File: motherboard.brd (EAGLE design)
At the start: 100 x 80 mm, 23 parts, among them U1 MC34063DIP

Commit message: Fix
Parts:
- moved I2C 1.27 mm to (96.5, 72.4)
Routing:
- net RX: track 110.6 -> 109.2 mm
- net TX: track 103.0 -> 101.8 mm
- net GND: track 346.7 -> 345.5 mm
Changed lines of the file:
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@@
 <element name="CON9" library="con-amp" package="SIMM22" value="" x="67.31" y="41.91" rot="R90"/>
 <element name="CON10" library="con-amp" package="SIMM22" value="" x="74.93" y="41.91" rot="R90"/>
-<element name="I2C" library="SparkFun-Connectors" package="AUDIO-JACK" value="" x="96.52" y="73.66" rot="R180"/>
+<element name="I2C" library="SparkFun-Connectors" package="AUDIO-JACK" value="" x="96.52" y="72.39" rot="R180"/>
 <element name="PWR" library="con-jack" package="DCJ0202" value="DCJ0202" x="88.9" y="59.69" rot="R90">
 <attribute name="OC_NEWARK" value="unknown" x="88.9" y="59.69" size="1.778" layer="27" rot="R90" display="off"/>
@@
 <wire x1="36.83" y1="50.8" x2="29.21" y2="50.8" width="1.4224" layer="16"/>
 <wire x1="74.93" y1="50.8" x2="81.28" y2="50.8" width="1.4224" layer="16"/>
-<wire x1="81.28" y1="50.8" x2="81.28" y2="68.66" width="1.4224" layer="16"/>
+<wire x1="81.28" y1="50.8" x2="81.28" y2="67.39" width="1.4224" layer="16"/>
 <contactref element="I2C" pad="RING"/>
-<wire x1="91.52" y1="68.66" x2="81.28" y2="68.66" width="1.4224" layer="16"/>
+<wire x1="91.52" y1="67.39" x2="81.28" y2="67.39" width="1.4224" layer="16"/>
 </signal>
 <signal name="RX">
@@
 <wire x1="67.31" y1="53.34" x2="74.93" y2="53.34" width="1.4224" layer="16"/>
 <wire x1="74.93" y1="53.34" x2="78.74" y2="53.34" width="1.4224" layer="16"/>
-<wire x1="78.74" y1="53.34" x2="78.74" y2="78.66" width="1.4224" layer="16"/>
+<wire x1="78.74" y1="53.34" x2="78.74" y2="77.39" width="1.4224" layer="16"/>
 <contactref element="I2C" pad="TIP"/>
-<wire x1="91.52" y1="78.66" x2="78.74" y2="78.66" width="1.4224" layer="16"/>
-<wire x1="78.74" y1="78.66" x2="78.74" y2="78.74" width="1.4224" layer="16"/>
+<wire x1="78.74" y1="73.58" x2="78.74" y2="77.47" width="0" layer="19" extent="1-16"/>
+<wire x1="91.52" y1="77.39" x2="78.74" y2="77.39" width="1.4224" layer="16"/>
+<wire x1="78.74" y1="77.39" x2="78.74" y2="73.58" width="0" layer="19" extent="1-16"/>
 </signal>
 <signal name="GND">
@@
 <wire x1="95.25" y1="40.64" x2="97.79" y2="40.64" width="1.4224" layer="16"/>
 <wire x1="97.79" y1="40.64" x2="97.79" y2="53.34" width="1.4224" layer="16"/>
-<wire x1="97.79" y1="53.34" x2="97.79" y2="73.66" width="1.4224" layer="16"/>
-<wire x1="97.79" y1="73.66" x2="96.52" y2="73.66" width="1.4224" layer="16"/>
+<wire x1="97.79" y1="53.34" x2="97.79" y2="72.39" width="1.4224" layer="16"/>
+<wire x1="97.79" y1="72.39" x2="96.52" y2="72.39" width="1.4224" layer="16"/>
 <wire x1="93.98" y1="53.34" x2="97.79" y2="53.34" width="1.4224" layer="16"/>
 <wire x1="29.21" y1="15.24" x2="36.83" y2="15.24" width="1.4224" layer="16"/>

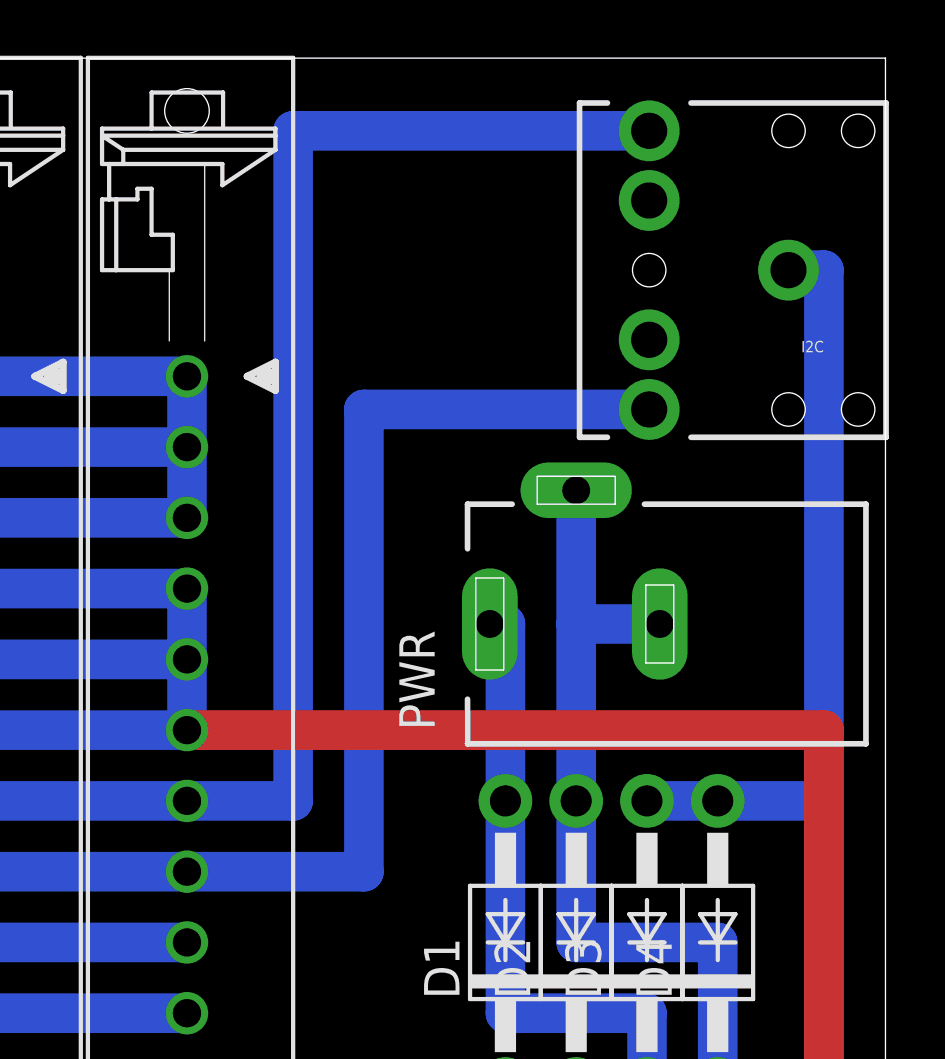
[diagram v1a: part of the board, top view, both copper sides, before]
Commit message: Added 3.3v regulator and circuit
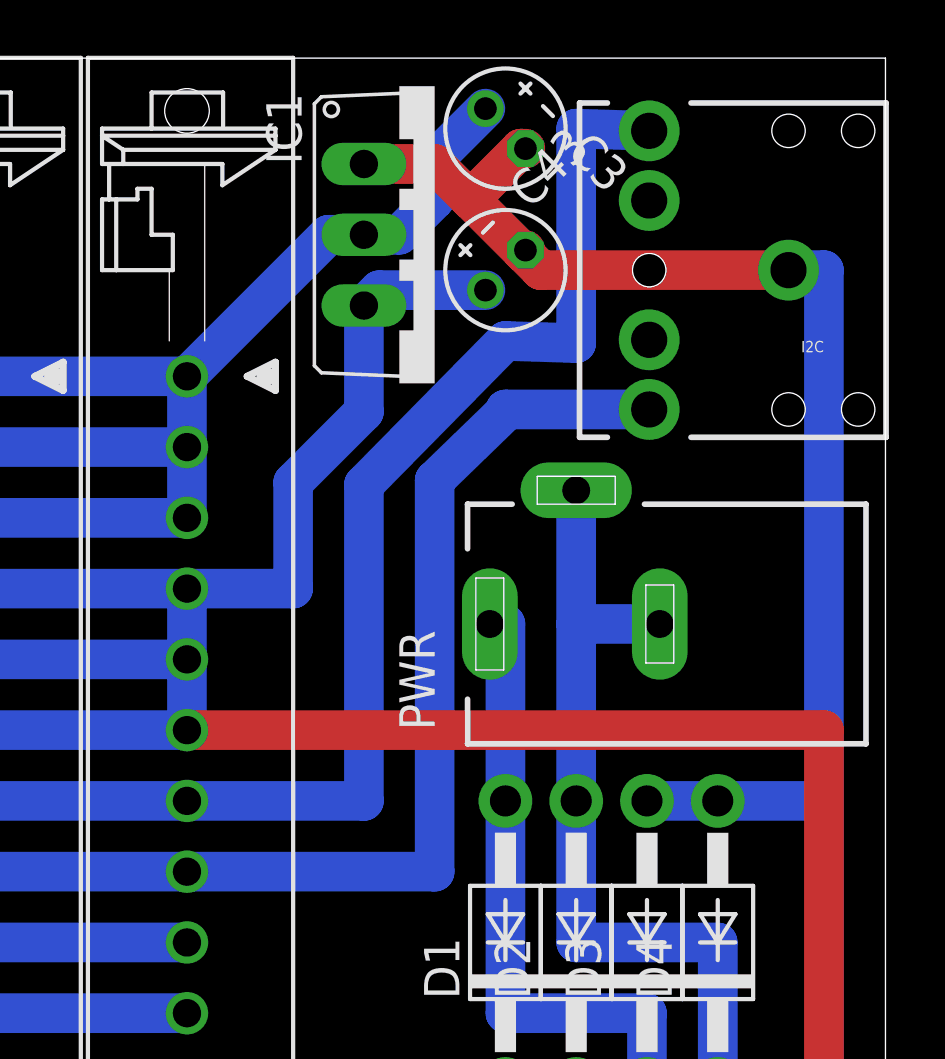
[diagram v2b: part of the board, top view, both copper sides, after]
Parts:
- added C3, C43: (no value), rcl:E2-4
- added IC1: MC33269T-3.3, linear:TO220V
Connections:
- net +3V3: now also C3.+, IC1.2
- net +5V: now also C43.+, IC1.3
- net GND: now also C3.-, C43.-, IC1.1
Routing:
- net GND: track 345.5 -> 365.2 mm
- net +5V: track 293.3 -> 313.0 mm
- net +3V3: track 210.8 -> 226.4 mm
- net RX: track 109.2 -> 106.4 mm
- net TX: track 101.8 -> 100.3 mm
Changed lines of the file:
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@@
 <element name="L1" library="rcl" package="0204/7" value="220uH" x="95.25" y="27.94" rot="R270"/>
 <element name="C2" library="rcl" package="E3,5-8" value="" x="92.71" y="8.89" rot="R45"/>
+<element name="IC1" library="linear" package="TO220V" value="MC33269T-3.3" x="83.82" y="73.66" rot="R270"/>
+<element name="C3" library="rcl" package="E2-4" value="" x="86.36" y="77.47" rot="R315"/>
+<element name="C43" library="rcl" package="E2-4" value="" x="86.36" y="72.39" rot="R45"/>
 </elements>
 <signals>
@@
 <wire x1="44.45" y1="50.8" x2="36.83" y2="50.8" width="1.4224" layer="16"/>
 <wire x1="36.83" y1="50.8" x2="29.21" y2="50.8" width="1.4224" layer="16"/>
-<wire x1="74.93" y1="50.8" x2="81.28" y2="50.8" width="1.4224" layer="16"/>
-<wire x1="81.28" y1="50.8" x2="81.28" y2="67.39" width="1.4224" layer="16"/>
+<wire x1="74.93" y1="50.8" x2="83.82" y2="50.8" width="1.4224" layer="16"/>
+<wire x1="83.82" y1="50.8" x2="83.82" y2="64.85" width="1.4224" layer="16"/>
 <contactref element="I2C" pad="RING"/>
-<wire x1="91.52" y1="67.39" x2="81.28" y2="67.39" width="1.4224" layer="16"/>
+<wire x1="91.52" y1="67.39" x2="86.36" y2="67.39" width="1.4224" layer="16"/>
+<wire x1="86.36" y1="67.39" x2="86.36" y2="67.31" width="1.4224" layer="16"/>
+<wire x1="86.36" y1="67.31" x2="83.82" y2="64.85" width="1.4224" layer="16"/>
 </signal>
 <signal name="RX">
@@
 <wire x1="59.69" y1="53.34" x2="67.31" y2="53.34" width="1.4224" layer="16"/>
 <wire x1="67.31" y1="53.34" x2="74.93" y2="53.34" width="1.4224" layer="16"/>
-<wire x1="74.93" y1="53.34" x2="78.74" y2="53.34" width="1.4224" layer="16"/>
-<wire x1="78.74" y1="53.34" x2="78.74" y2="77.39" width="1.4224" layer="16"/>
+<wire x1="74.93" y1="53.34" x2="81.28" y2="53.34" width="1.4224" layer="16"/>
+<wire x1="81.28" y1="53.34" x2="81.28" y2="64.69" width="1.4224" layer="16"/>
+<wire x1="81.28" y1="64.69" x2="86.36" y2="69.85" width="1.4224" layer="16"/>
+<wire x1="86.36" y1="69.85" x2="88.9" y2="69.77" width="1.4224" layer="16"/>
 <contactref element="I2C" pad="TIP"/>
-<wire x1="78.74" y1="73.58" x2="78.74" y2="77.47" width="0" layer="19" extent="1-16"/>
-<wire x1="91.52" y1="77.39" x2="78.74" y2="77.39" width="1.4224" layer="16"/>
-<wire x1="78.74" y1="77.39" x2="78.74" y2="73.58" width="0" layer="19" extent="1-16"/>
+<wire x1="91.52" y1="77.39" x2="88.9" y2="77.47" width="1.4224" layer="16"/>
+<wire x1="88.9" y1="77.47" x2="88.9" y2="69.77" width="1.4224" layer="16"/>
 </signal>
 <signal name="GND">
@@
 <wire x1="93.98" y1="19.037234375" x2="93.98" y2="21.59" width="1.4224" layer="16"/>
 <wire x1="93.967234375" y1="10.147234375" x2="97.79" y2="10.147234375" width="1.4224" layer="16"/>
+<contactref element="IC1" pad="1"/>
+<contactref element="C43" pad="-"/>
+<contactref element="C3" pad="-"/>
+<wire x1="96.52" y1="72.39" x2="87.63" y2="72.39" width="1.4224" layer="1"/>
+<wire x1="87.63" y1="72.39" x2="86.995" y2="73.025" width="1.4224" layer="1"/>
+<wire x1="86.995" y1="73.025" x2="85.09" y2="74.93" width="1.4224" layer="1"/>
+<wire x1="85.09" y1="74.93" x2="83.82" y2="76.2" width="1.4224" layer="1"/>
+<wire x1="81.28" y1="76.2" x2="83.82" y2="76.2" width="1.4224" layer="1"/>
+<wire x1="87.07841875" y1="76.751578125" x2="86.911578125" y2="76.751578125" width="1.4224" layer="1"/>
+<wire x1="86.911578125" y1="76.751578125" x2="85.09" y2="74.93" width="1.4224" layer="1"/>
+<wire x1="87.07841875" y1="73.10841875" x2="86.995" y2="73.025" width="1.4224" layer="1"/>
 </signal>
 <signal name="+3V3">
@@
 <wire x1="74.93" y1="63.5" x2="74.93" y2="66.04" width="1.4224" layer="16"/>
 <wire x1="74.93" y1="66.04" x2="74.93" y2="68.58" width="1.4224" layer="16"/>
+<contactref element="IC1" pad="2"/>
+<contactref element="C3" pad="+"/>
+<wire x1="81.28" y1="73.66" x2="80.01" y2="73.66" width="1.4224" layer="16"/>
+<wire x1="80.01" y1="73.66" x2="74.93" y2="68.58" width="1.4224" layer="16"/>
+<wire x1="81.28" y1="73.66" x2="82.55" y2="73.66" width="1.4224" layer="16"/>
+<wire x1="82.55" y1="73.66" x2="83.82" y2="74.93" width="1.4224" layer="16"/>
+<wire x1="83.82" y1="74.93" x2="83.82" y2="76.366840625" width="1.4224" layer="16"/>
+<wire x1="83.82" y1="76.366840625" x2="85.641578125" y2="78.18841875" width="1.4224" layer="16"/>
 </signal>
 <signal name="+5V">
@@
 <wire x1="91.4527625" y1="13.97" x2="97.79" y2="13.97" width="1.4224" layer="1"/>
 <wire x1="97.79" y1="13.97" x2="97.79" y2="31.75" width="1.4224" layer="1"/>
+<contactref element="IC1" pad="3"/>
+<contactref element="C43" pad="+"/>
+<wire x1="81.28" y1="71.12" x2="81.28" y2="67.31" width="1.4224" layer="16"/>
+<wire x1="81.28" y1="67.31" x2="78.74" y2="64.77" width="1.4224" layer="16"/>
+<wire x1="78.74" y1="64.77" x2="78.74" y2="60.96" width="1.4224" layer="16"/>
+<wire x1="78.74" y1="60.96" x2="74.93" y2="60.96" width="1.4224" layer="16"/>
+<wire x1="85.641578125" y1="71.671578125" x2="81.831578125" y2="71.671578125" width="1.4224" layer="16"/>
+<wire x1="81.831578125" y1="71.671578125" x2="81.28" y2="71.12" width="1.4224" layer="16"/>
 </signal>
 <signal name="+12VL">
